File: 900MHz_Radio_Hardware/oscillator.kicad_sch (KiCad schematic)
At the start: 20 parts, among them SW1 SW_SPDT, U4 Opamp_Dual

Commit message: Completed oscillator
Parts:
- added C13: 100n, symbol Device:C
- added C14: 220n, symbol Device:C
- added C15: 470n, symbol Device:C
- added C22: 0.1u, symbol Device:C
- added R7: 10k, symbol Device:R
- added U5: ~, Package_TO_SOT_SMD:SOT-23-6_Handsoldering, symbol MRDT_ICs:BD0926
- U4: footprint (none) -> Package_SO:SOIC-8_3.9x4.9mm_P1.27mm
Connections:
- net +5V: now also C22.1
- net GNDA: now also C13.2, C14.2, C15.2
- net GNDPWR: now also C11.2, C12.2, C9.2, C13.1, C14.1, C15.1, C22.2, U5.2 (GND), U5.4 (GND), U5.6 (GND); no longer C11.1, C12.1, C9.1
- net at R6.2, R7.2, U4.3 (+): now also R7.2
- net OSC_IN: now reaches U3.2 (TUNE), U4.6 (-), U4.7
- net OSC_IN: now also C11.1, C12.1, C9.1; no longer C11.2, C12.2, C9.2
- net OSC_VCC: now reaches C4.1, C5.1, C7.1, R3.1, SW1.3 (C), U3.5 (VCC), U3.6 (VCC)
- net OSC_CTL_A renamed CTL_A
- net OSC_CTL_B renamed CTL_B
- net OSC_ENB renamed ENB
- net OSC_OUT renamed OSC_RAW_OUT
- net OSC_RAW_OUT: now also U5.5 (IN)
- new net CTL_C: R7.1
- new net OSC_OUT1: U5.1 (P1)
- new net OSC_OUT2: U5.3 (P2)
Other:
- note added: "Power Divider"
- moved on the sheet: C11, C12, C4, C5, C7, C9, D3, D4, R3, R4, U4C

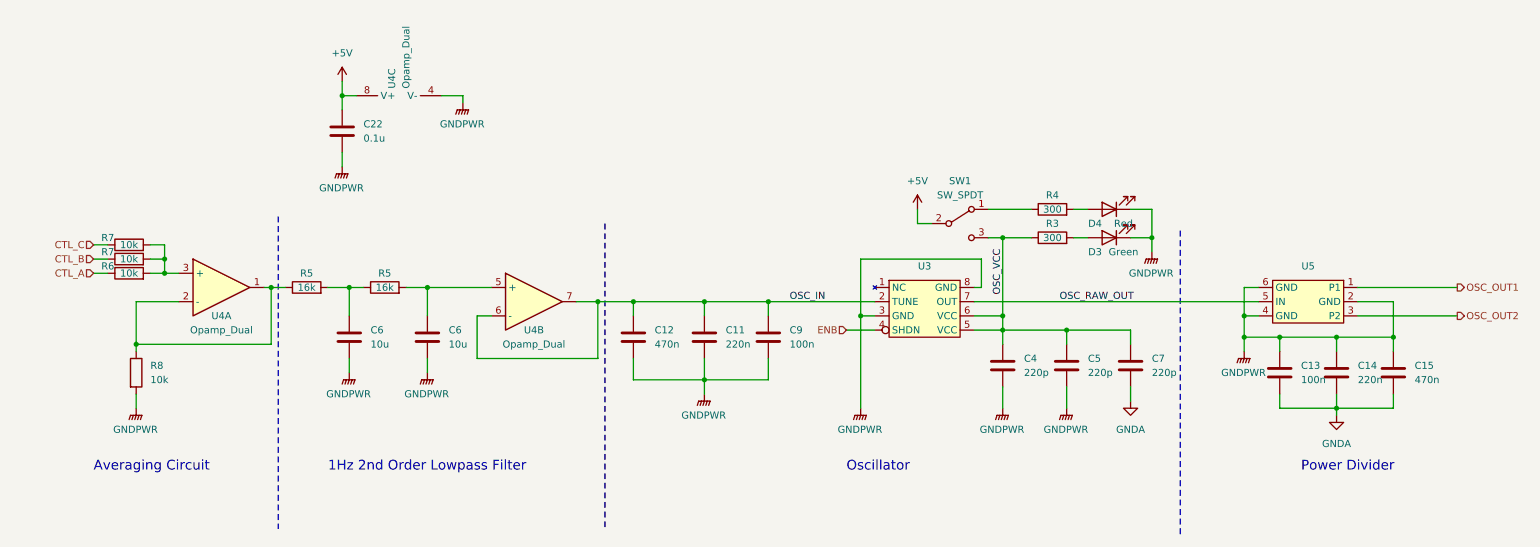
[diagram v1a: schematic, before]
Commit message: Replaced oscillator Tune circuit
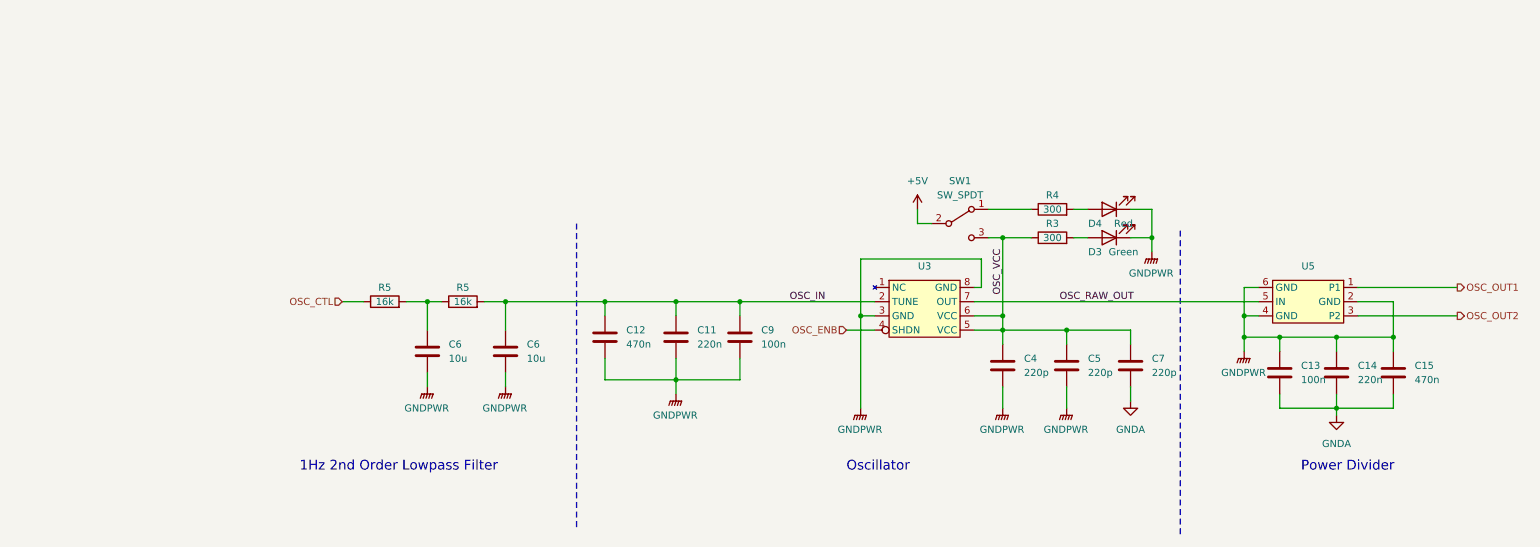
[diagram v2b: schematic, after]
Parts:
- removed C22: 0.1u, symbol Device:C
- removed R6, R7 (x2), R8: 10k, symbol Device:R
- removed U4: Opamp_Dual, Package_SO:SOIC-8_3.9x4.9mm_P1.27mm, symbol Device:Opamp_Dual
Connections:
- net OSC_IN: now also C6.1, R5.2
- net OSC_CTL: now reaches R5.1
- net ENB renamed OSC_ENB
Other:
- note removed: "Averaging Circuit"
- moved on the sheet: C11, C12, C6, C9, R5
